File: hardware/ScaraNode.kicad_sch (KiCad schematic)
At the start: 39 parts, among them J1 FIM1, J2 FIM2, J3 NTC, J4 DM556, J5 24V, J6 MOTOR, J7 FAN 24V, U1 RP2040-Zero, U2 74ACT245, U4 TMC2209

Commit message: docs(placa): publica ScaraNode v18
- Canais independentes: TMC2209 em GP4/GP5/GP0 e DM556 em GP6/GP7/GP8;
  uma placa pode mover dois motores ao mesmo tempo.
- UART do TMC2209 no pino 4 do soquete (GP2 via JU); ate a v17 ia ao pino 5.
- Sem o jumper ZM (MS1/MS2 fixos, endereco UART 3).
- Segundo NTC (J8, GP26) e segunda saida de ventoinha (J9).
- Nenhuma curva de trilha de 90 graus.
- Fusivel de 2 A por placa (e 5 A por DM556) numa caixa de fusiveis de
  lamina, documentado no capitulo 6; avisos para nao queimar o driver no
  cfg e no capitulo 7.
- Validada: 128 pinos, ERC e paridade 0, DRC de cobre sem erro.

Co-Authored-By: Claude Opus 5.5 <noreply@anthropic.com>
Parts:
- removed ZM: MICROPASSO, Connector_PinHeader_2.54mm:PinHeader_2x03_P2.54mm_Vertical, symbol Connector_Generic:Conn_02x03_Odd_Even
- added C7: 100nF, Capacitor_THT:C_Disc_D3.0mm_W1.6mm_P2.50mm, symbol Device:C
- added J8: NTC2, Connector_JST:JST_XH_B2B-XH-A_1x02_P2.50mm_Vertical, symbol Connector_Generic:Conn_01x02
- added J9: FAN2 24V, Connector_JST:JST_XH_B2B-XH-A_1x02_P2.50mm_Vertical, symbol Connector_Generic:Conn_01x02
- added R15: 100k, Resistor_THT:R_Axial_DIN0207_L6.3mm_D2.5mm_P10.16mm_Horizontal, symbol Device:R
- J3: value NTC -> NTC1
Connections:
- net MS3 is gone; now on net UART_TMC: R7.1, U4.4 (MS3/UART)
- net 24V: now also J9.1 (Pin_1)
- net 3V3: now also R15.1
- net DIR: now also U1.GP5; no longer U1.GP7, U2.17 (B2)
- net GND: now also C7.2, J8.2 (Pin_2), J9.2 (Pin_2)
- net STP: now also U1.GP4; no longer U1.GP6, U2.18 (B1)
- net UART: now also U1.GP2; no longer U1.GP5
- net UART_TMC: no longer U4.5 (RST/PDN)
- net NTC2: now reaches U1.GP26
- net NTC2: now also C7.1, J8.1 (Pin_1), R15.2
- new net DM_DIR: U1.GP7, U2.17 (B2)
- new net DM_STP: U1.GP6, U2.18 (B1)
- no-connect marks 12 -> 10

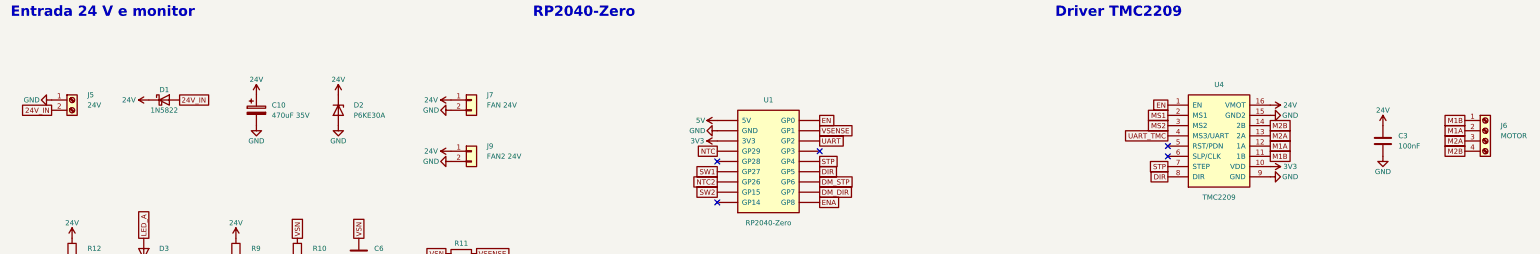
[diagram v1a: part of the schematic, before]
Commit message: docs(placa): conectores plugaveis 2EDG e furos M3 esquadrados (v18)
- J5 24 V: 2EDGRC 90 graus + plugue 2EDGK, entrando pela borda de cima.
- J6 motor: 2EDGVC vertical + plugue 2EDGK, fio saindo para a direita.
- Os quatro furos M3 nos cantos (retangulo de 69 x 57 mm); DXF atualizado.
- C10 a 1,4 mm do J5. Validada: 128 pinos, DRC de cobre sem erro.

Co-Authored-By: Claude Opus 5.5 <noreply@anthropic.com>
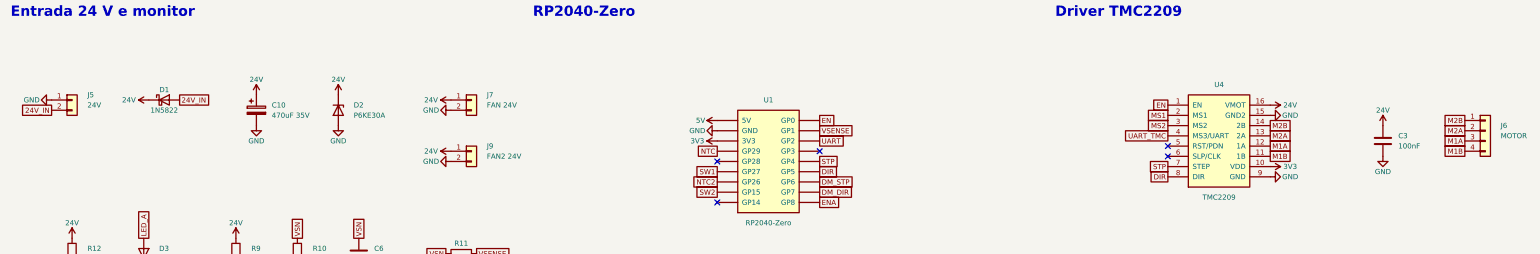
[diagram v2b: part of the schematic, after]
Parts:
- J5: footprint TerminalBlock_Phoenix:TerminalBlock_Phoenix_MKDS-1,5-2-5.08_1x02_P5.08mm_Horizontal -> Connector_Phoenix_MSTB:PhoenixContact_MSTBA_2,5_2-G-5,08_1x02_P5.08mm_Horizontal; symbol Connector:Screw_Terminal_01x02 -> Connector_Generic:Conn_01x02
- J6: footprint TerminalBlock_Phoenix:TerminalBlock_Phoenix_MKDS-1,5-4-5.08_1x04_P5.08mm_Horizontal -> Connector_Phoenix_MSTB:PhoenixContact_MSTBVA_2,5_4-G-5,08_1x04_P5.08mm_Vertical; symbol Connector:Screw_Terminal_01x04 -> Connector_Generic:Conn_01x04
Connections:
- net M1A: now also J6.3 (Pin_3); no longer J6.2 (Pin_2)
- net M1B: now also J6.4 (Pin_4); no longer J6.1 (Pin_1)
- net M2A: now also J6.2 (Pin_2); no longer J6.3 (Pin_3)
- net M2B: now also J6.1 (Pin_1); no longer J6.4 (Pin_4)
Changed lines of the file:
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@@
 	)
 	(symbol
-		(lib_id "Connector:Screw_Terminal_01x02")
+		(lib_id "Connector_Generic:Conn_01x02")
 		(at 38.1 50.8 0)
 		(unit 1)
@@
 			)
 		)
-		(property "Footprint" "TerminalBlock_Phoenix:TerminalBlock_Phoenix_MKDS-1,5-2-5.08_1x02_P5.08mm_Horizontal"
+		(property "Footprint" "Connector_Phoenix_MSTB:PhoenixContact_MSTBA_2,5_2-G-5,08_1x02_P5.08mm_Horizontal"
 			(at 38.1 50.8 0)
 			(effects
@@
 	)
 	(symbol
-		(lib_id "Connector:Screw_Terminal_01x04")
+		(lib_id "Connector_Generic:Conn_01x04")
 		(at 388.62 58.42 0)
 		(unit 1)
@@
 			)
 		)
-		(property "Footprint" "TerminalBlock_Phoenix:TerminalBlock_Phoenix_MKDS-1,5-4-5.08_1x04_P5.08mm_Horizontal"
+		(property "Footprint" "Connector_Phoenix_MSTB:PhoenixContact_MSTBVA_2,5_4-G-5,08_1x04_P5.08mm_Vertical"
 			(at 388.62 58.42 0)
 			(effects
@@
 		)
 	)
+	(global_label "M2B"
+		(shape passive)
+		(at 383.54 55.88 180)
+		(effects
+			(font
+				(size 1.27 1.27)
+			)
+			(justify right)
+		)
+	)
+	(global_label "M2A"
+		(shape passive)
+		(at 383.54 58.42 180)
+		(effects
+			(font
+				(size 1.27 1.27)
+			)
+			(justify right)
+		)
+	)
+	(global_label "M1A"
+		(shape passive)
+		(at 383.54 60.96 180)
+		(effects
+			(font
+				(size 1.27 1.27)
+			)
+			(justify right)
+		)
+	)
 	(global_label "M1B"
 		(shape passive)
-		(at 383.54 55.88 180)
-		(effects
-			(font
-				(size 1.27 1.27)
-			)
-			(justify right)
-		)
-	)
-	(global_label "M1A"
-		(shape passive)
-		(at 383.54 58.42 180)
-		(effects
-			(font
-				(size 1.27 1.27)
-			)
-			(justify right)
-		)
-	)
-	(global_label "M2A"
-		(shape passive)
-		(at 383.54 60.96 180)
-		(effects
-			(font
-				(size 1.27 1.27)
-			)
-			(justify right)
-		)
-	)
-	(global_label "M2B"
-		(shape passive)
 		(at 383.54 63.5 180)
